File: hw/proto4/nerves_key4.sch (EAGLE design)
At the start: 3 parts, among them U1 ATECC508A-SSHDA

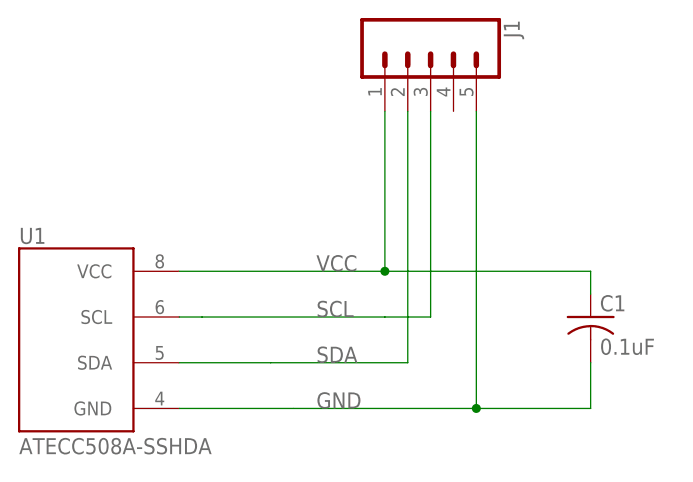
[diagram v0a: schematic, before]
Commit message: Fix ERC/DRC
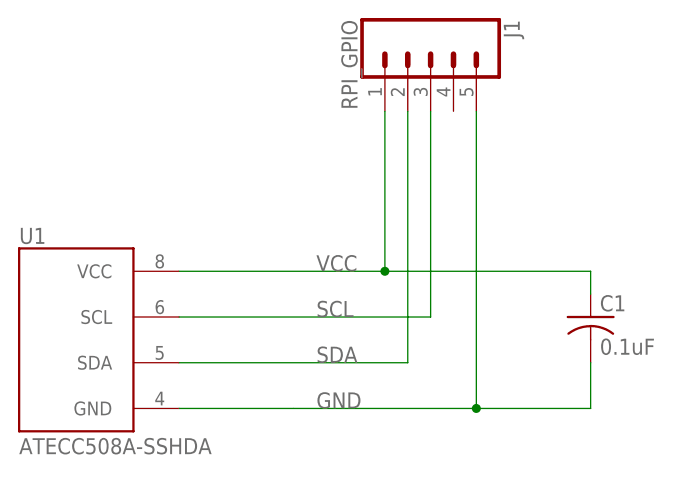
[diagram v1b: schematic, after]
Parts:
- J1: value (none) -> RPI_GPIO
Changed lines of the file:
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@@
 <part name="U1" library="cryptopi" deviceset="ATECC508A" device="SOIC-8-NARROW" package3d_urn="urn:adsk.eagle:package:4514464/1" value="ATECC508A-SSHDA"/>
 <part name="FRAME1" library="frames" library_urn="urn:adsk.eagle:library:229" deviceset="FRAME_A_L" device="" value="FRAME1"/>
-<part name="J1" library="SparkFun-Connectors" library_urn="urn:adsk.eagle:library:513" deviceset="CONN_05" device="" package3d_urn="urn:adsk.eagle:package:38104/1"/>
+<part name="J1" library="SparkFun-Connectors" library_urn="urn:adsk.eagle:library:513" deviceset="CONN_05" device="" package3d_urn="urn:adsk.eagle:package:38104/1" value="RPI_GPIO"/>
 </parts>
 <sheets>
@@
 <net name="VCC" class="0">
 <segment>
+<label x="116.84" y="129.54" size="1.778" layer="95"/>
+<pinref part="J1" gate="G$1" pin="1"/>
+<wire x1="124.46" y1="129.54" x2="124.46" y2="147.32" width="0.1524" layer="91"/>
 <pinref part="U1" gate="G$1" pin="VCC"/>
 <wire x1="101.6" y1="129.54" x2="124.46" y2="129.54" width="0.1524" layer="91"/>
-<label x="116.84" y="129.54" size="1.778" layer="95"/>
-<wire x1="124.46" y1="129.54" x2="127" y2="129.54" width="0.1524" layer="91"/>
 <pinref part="C1" gate="G$1" pin="1"/>
-<wire x1="129.54" y1="129.54" x2="127" y2="129.54" width="0.1524" layer="91"/>
-<wire x1="147.32" y1="127" x2="147.32" y2="129.54" width="0.1524" layer="91"/>
-<wire x1="147.32" y1="129.54" x2="129.54" y2="129.54" width="0.1524" layer="91"/>
-<pinref part="J1" gate="G$1" pin="1"/>
-<wire x1="124.46" y1="129.54" x2="124.46" y2="147.32" width="0.1524" layer="91"/>
+<wire x1="124.46" y1="129.54" x2="147.32" y2="129.54" width="0.1524" layer="91"/>
+<wire x1="147.32" y1="129.54" x2="147.32" y2="127" width="0.1524" layer="91"/>
 <junction x="124.46" y="129.54"/>
-</segment>
-</net>
-<net name="SCL" class="0">
-<segment>
-<pinref part="U1" gate="G$1" pin="SCL"/>
-<wire x1="101.6" y1="124.46" x2="104.14" y2="124.46" width="0.1524" layer="91"/>
-<label x="116.84" y="124.46" size="1.778" layer="95"/>
-<wire x1="124.46" y1="124.46" x2="104.14" y2="124.46" width="0.1524" layer="91"/>
-<pinref part="J1" gate="G$1" pin="3"/>
-<wire x1="124.46" y1="124.46" x2="129.54" y2="124.46" width="0.1524" layer="91"/>
-<wire x1="129.54" y1="124.46" x2="129.54" y2="147.32" width="0.1524" layer="91"/>
 </segment>
 </net>
 <net name="SDA" class="0">
 <segment>
-<pinref part="U1" gate="G$1" pin="SDA"/>
-<wire x1="101.6" y1="119.38" x2="111.76" y2="119.38" width="0.1524" layer="91"/>
 <label x="116.84" y="119.38" size="1.778" layer="95"/>
 <pinref part="J1" gate="G$1" pin="2"/>
-<wire x1="127" y1="119.38" x2="111.76" y2="119.38" width="0.1524" layer="91"/>
+<wire x1="127" y1="119.38" x2="101.6" y2="119.38" width="0.1524" layer="91"/>
 <wire x1="127" y1="119.38" x2="127" y2="147.32" width="0.1524" layer="91"/>
+<pinref part="U1" gate="G$1" pin="SDA"/>
 </segment>
 </net>
@@
 </segment>
 </net>
+<net name="SCL" class="0">
+<segment>
+<pinref part="U1" gate="G$1" pin="SCL"/>
+<pinref part="J1" gate="G$1" pin="3"/>
+<wire x1="101.6" y1="124.46" x2="129.54" y2="124.46" width="0.1524" layer="91"/>
+<wire x1="129.54" y1="124.46" x2="129.54" y2="147.32" width="0.1524" layer="91"/>
+<label x="116.84" y="124.46" size="1.778" layer="95"/>
+</segment>
+</net>
